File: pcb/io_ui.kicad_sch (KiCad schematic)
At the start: 27 parts, among them J10 UART, J4 Digital IO, J5 ADC Inputs, J8 I2C Bus, Q4 2N7002, Q5 2N7002, U6 128x32 OLED, U8 24AA64T

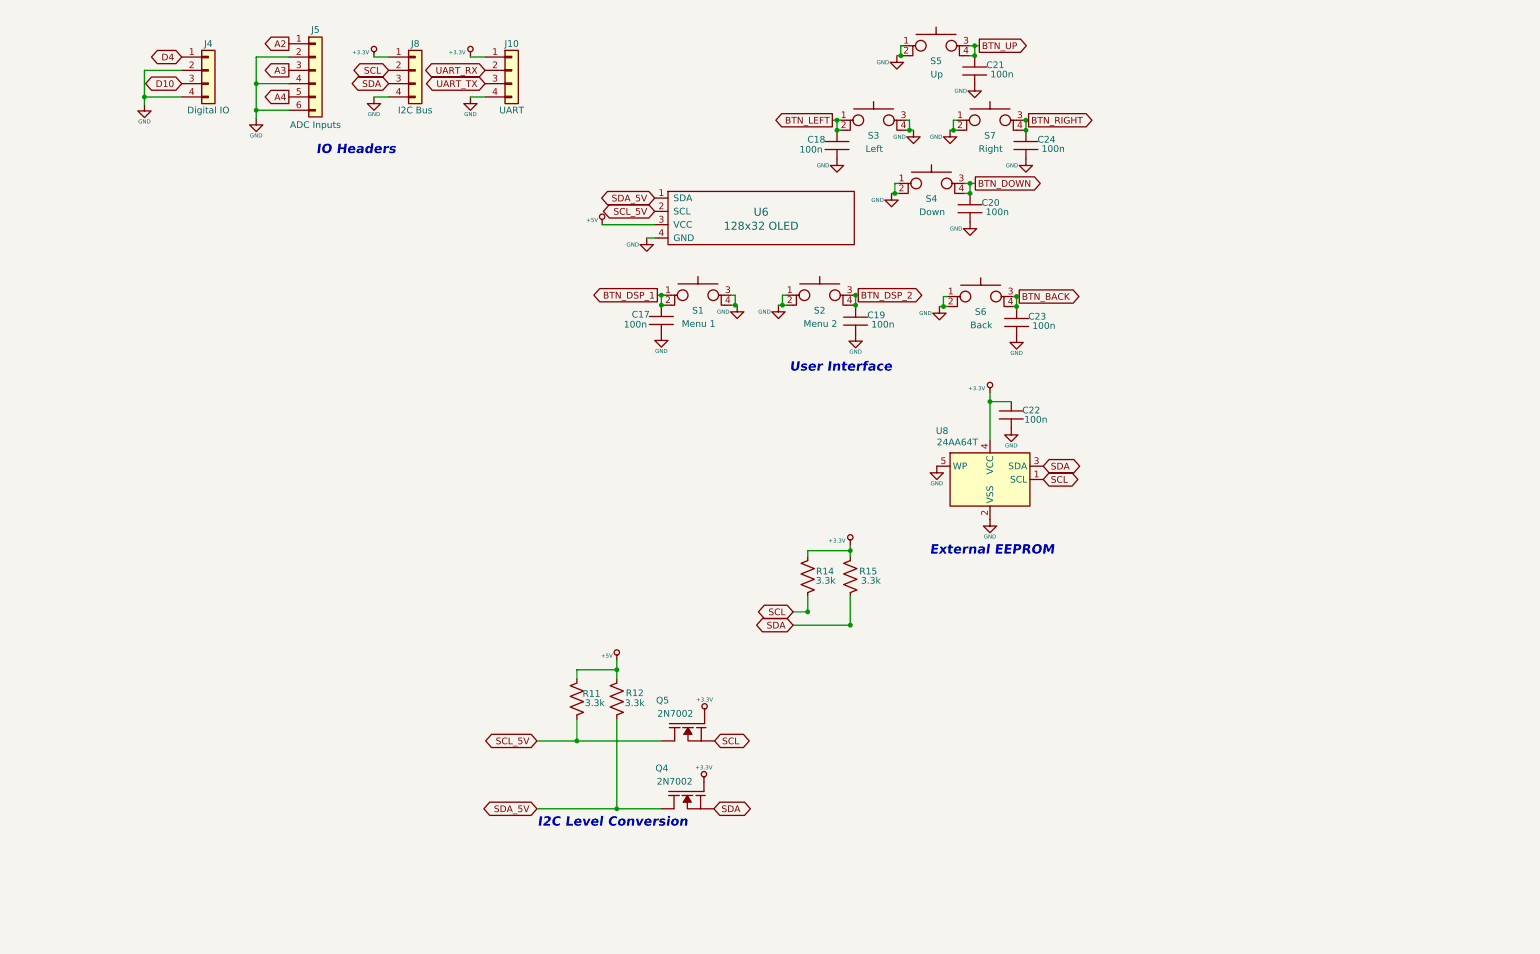
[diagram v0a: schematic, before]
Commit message: UI: 128x32 I2C OLED -> 1.3in SH1106 SPI 7-pin DS1 (as Si5351AVFO, DNP) on SPI1 ALT1 PC4/PC6 + CS PC7, DC PB4, RES PB5; FB1+C25-C27 rail filter; VFO 10k/10k/100n RC on all 7 buttons (R50-R63); D-pad stays PD3-PD6; layout note; regen PDF
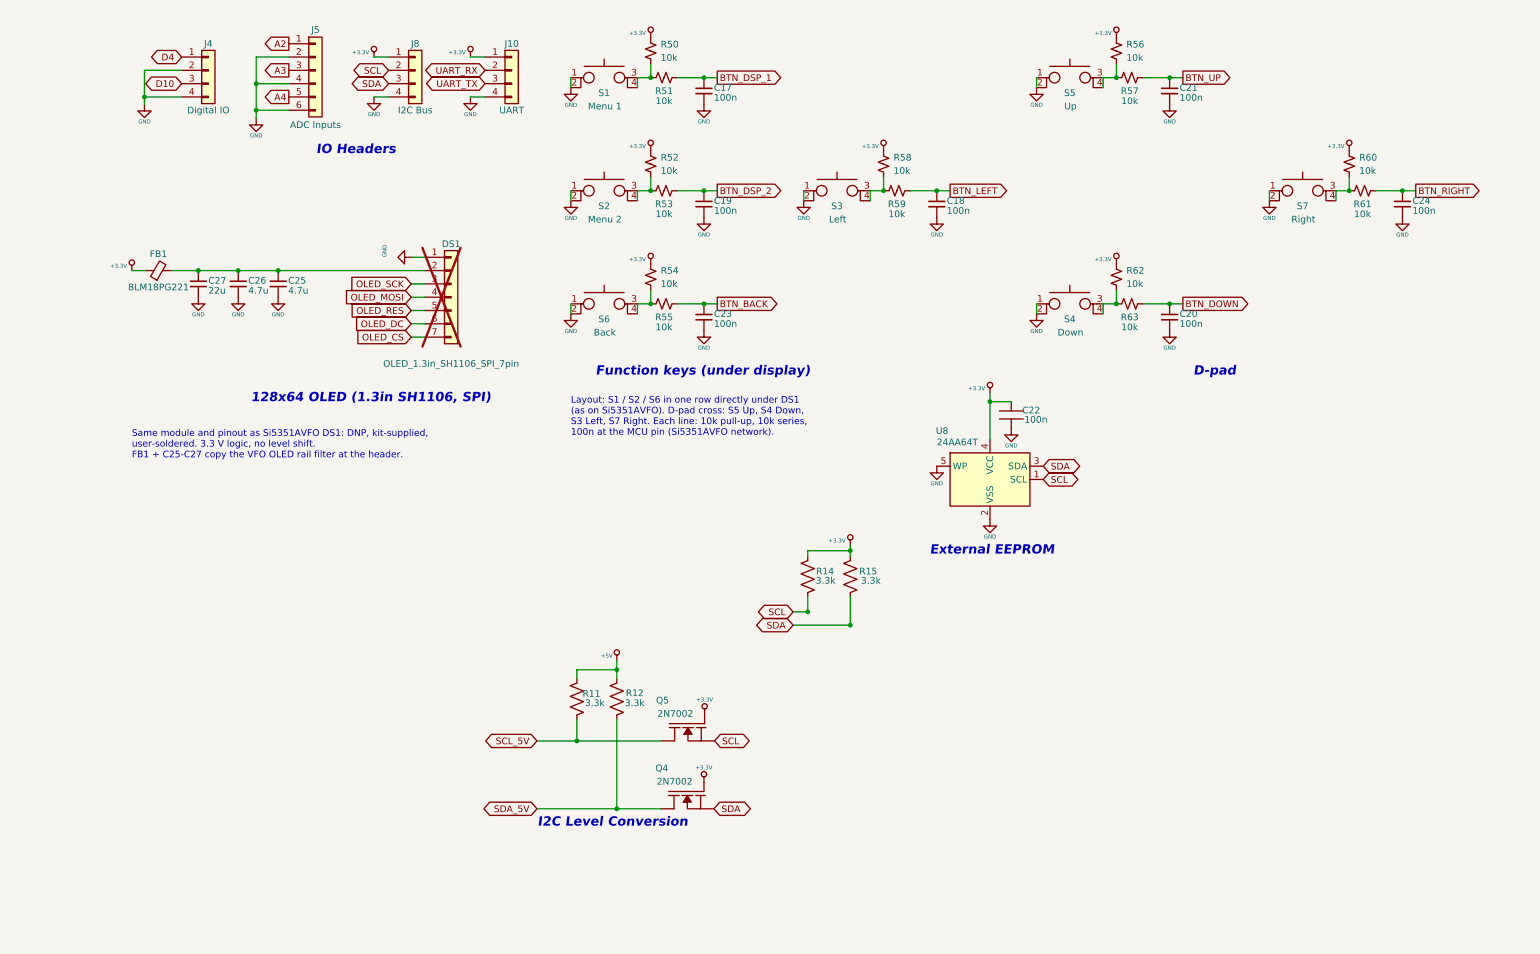
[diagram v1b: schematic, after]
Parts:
- removed C17, C18, C19, C20, C21, C23, C24: 100n, Capacitor_SMD:C_0805_2012Metric, symbol EtherkitKicadLibrary:C
- removed U6: 128x32 OLED, EtherkitKicadLibrary:128x32OLED, symbol EtherkitKicadLibrary:128x32OLED
- added C17, C18, C19, C20, C21, C23, C24: 100n, Capacitor_SMD:C_0805_2012Metric, symbol Device:C_Small
- added C25, C26: 4.7u, Capacitor_SMD:C_0805_2012Metric, symbol Device:C_Small
- added C27: 22u, Capacitor_SMD:C_1206_3216Metric, symbol Device:C_Small
- added DS1: OLED_1.3in_SH1106_SPI_7pin, Connector_PinHeader_2.54mm:PinHeader_1x07_P2.54mm_Vertical, symbol Connector_Generic:Conn_01x07
- added FB1: BLM18PG221, Inductor_SMD:L_0603_1608Metric, symbol Device:FerriteBead_Small
- added R50, R51, R52, R53, R54, R55, R56, R57, R58, R59, R60, R61, R62, R63: 10k, Resistor_SMD:R_0805_2012Metric, symbol Device:R_Small_US
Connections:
- net +3.3V: now also FB1.1, R50.1, R52.1, R54.1, R56.1, R58.1, R60.1, R62.1
- net BTN_BACK: now also C23.1, R55.2; no longer S6.3, S6.4
- net BTN_DOWN: now also C20.1, R63.2; no longer S4.3, S4.4
- net BTN_DSP_1: now also C17.1, R51.2; no longer S1.1, S1.2
- net BTN_DSP_2: now also C19.1, R53.2; no longer S2.3, S2.4
- net BTN_LEFT: now also C18.1, R59.2; no longer S3.1, S3.2
- net BTN_RIGHT: now also C24.1, R61.2; no longer S7.3, S7.4
- net BTN_UP: now also C21.1, R57.2; no longer S5.3, S5.4
- net GND: now also S1.1, S1.2, S3.1, S3.2, C17.2, C18.2, C19.2, C20.2, C21.2, C23.2, C24.2, C25.2, C26.2, C27.2, DS1.1 (Pin_1); no longer S1.3, S1.4, S3.3, S3.4
- new net: R56.2, R57.1, S5.3, S5.4
- new net: R58.2, R59.1, S3.3, S3.4
- new net: R60.2, R61.1, S7.3, S7.4
- new net: R62.2, R63.1, S4.3, S4.4
- new net: R50.2, R51.1, S1.3, S1.4
- new net: R52.2, R53.1, S2.3, S2.4
- new net: R54.2, R55.1, S6.3, S6.4
- new net: C25.1, C26.1, C27.1, DS1.2 (Pin_2), FB1.2
- new net OLED_CS: DS1.7 (Pin_7)
- new net OLED_DC: DS1.6 (Pin_6)
- new net OLED_MOSI: DS1.4 (Pin_4)
- new net OLED_RES: DS1.5 (Pin_5)
- new net OLED_SCK: DS1.3 (Pin_3)
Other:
- note added: "128x64 OLED (1.3in SH1106, SPI)"
- note added: "D-pad"
- note added: "Function keys (under display)"
- note added: "Layout: S1 / S2 / S6 in one row directly under DS1 (as on Si5351AVFO). D-pad cross: S5 Up, S4 Down, S3 Left, S7 Right. Each line: 10k pull-up, 10k series, 100n at the MCU pin (Si5351AVFO network)."
- note added: "Same module and pinout as Si5351AVFO DS1: DNP, kit-supplied, user-soldered. 3.3 V logic, no level shift. FB1 + C25-C27 copy the VFO OLED rail filter at the header."
- note removed: "User Interface"
- moved on the sheet: S1, S2, S3, S4, S5, S6, S7

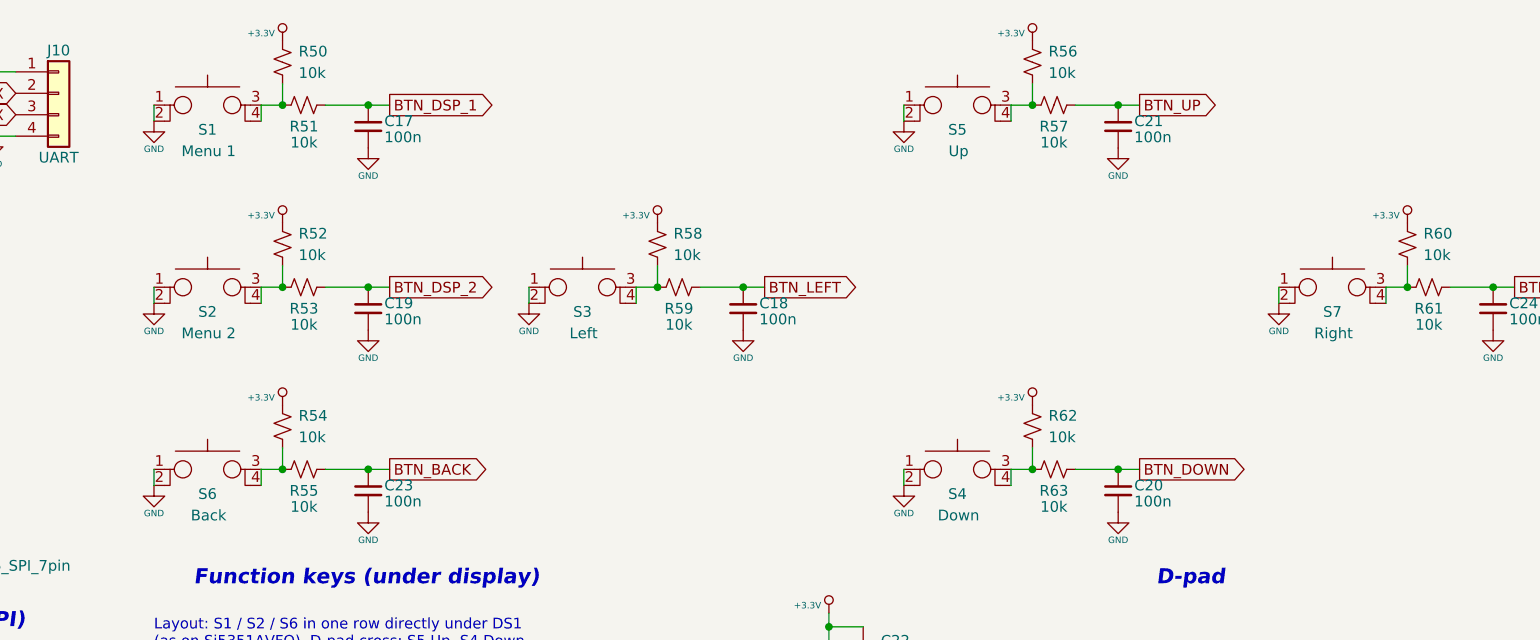
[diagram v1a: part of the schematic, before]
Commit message: UI: S1-S7 Omron B3F (4-pin) -> Kinghelm KH-6X6X11H-STM C2837537 as on Si5351AVFO (Switch:SW_Push 2-pin, OB2:SW_Push_6x6mm_SMD_KH-6X6X11H-STM footprint copied from VFO lib); pin1=GND, pin2=RC net; nets unchanged; regen PDF
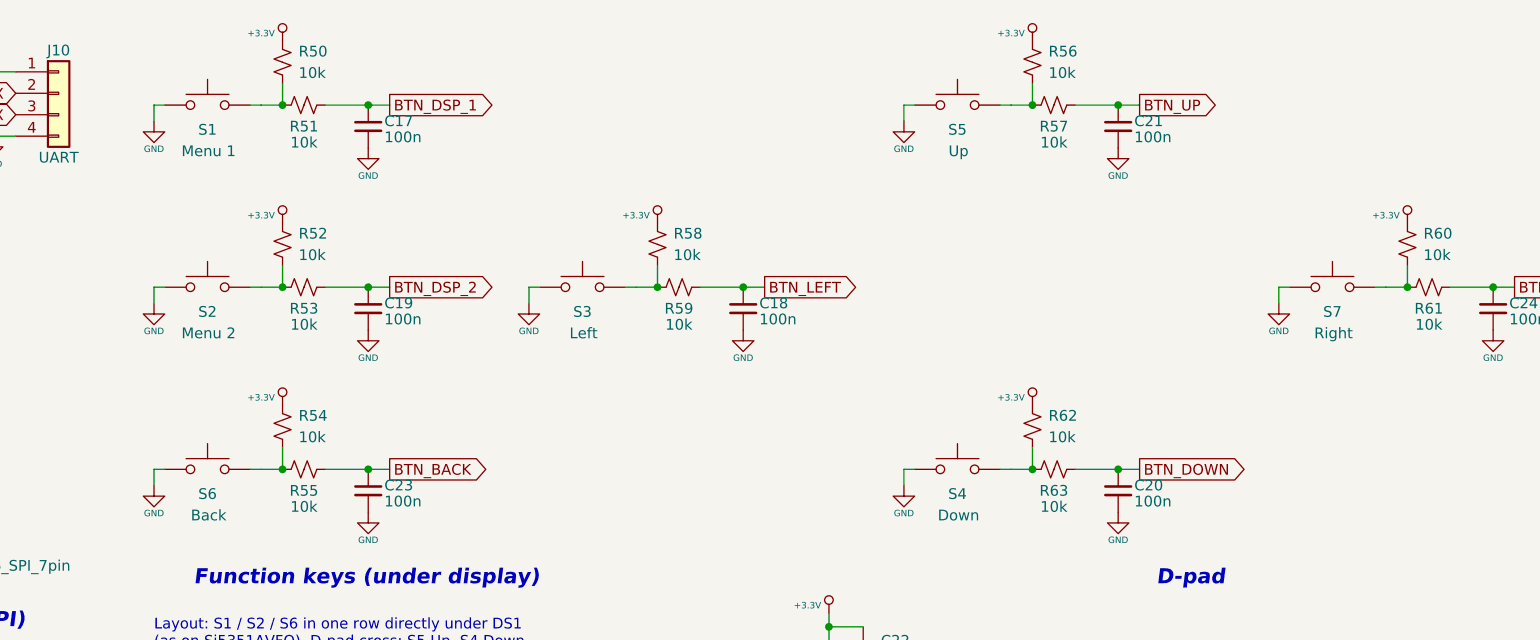
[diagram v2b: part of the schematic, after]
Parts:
- S1, S2, S3, S4, S5, S6, S7: footprint EtherkitKicadLibrary:Omron_B3F-1052 -> OB2:SW_Push_6x6mm_SMD_KH-6X6X11H-STM; symbol EtherkitKicadLibrary:PUSHBUTTON_TACTILE -> Switch:SW_Push; LCSC (none) -> C2837537; MPN (none) -> KH-6X6X11H-STM; Manufacturer (none) -> Kinghelm
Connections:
- net GND: no longer S1.2, S2.2, S3.2, S4.2, S5.2, S6.2, S7.2
- net at R56.2, R57.1: now also S5.2; no longer S5.3, S5.4
- net at R58.2, R59.1: now also S3.2; no longer S3.3, S3.4
- net at R60.2, R61.1: now also S7.2; no longer S7.3, S7.4
- net at R62.2, R63.1: now also S4.2; no longer S4.3, S4.4
- net at R50.2, R51.1: now also S1.2; no longer S1.3, S1.4
- net at R52.2, R53.1: now also S2.2; no longer S2.3, S2.4
- net at R54.2, R55.1: now also S6.2; no longer S6.3, S6.4

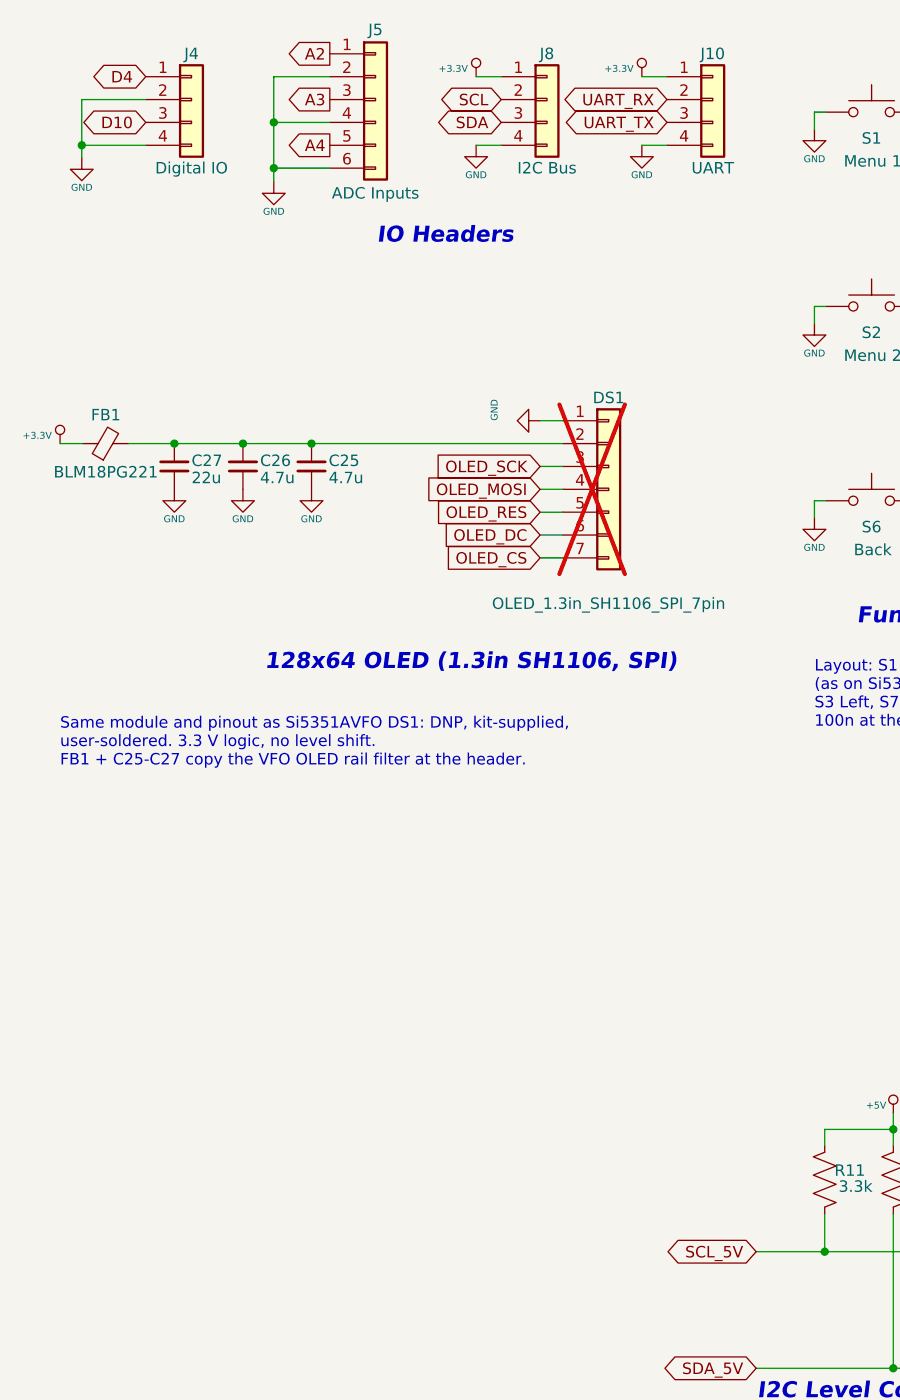
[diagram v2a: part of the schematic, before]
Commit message: IO: Option B spare GPIO - J4 1x10 (D7/PA7, D17/PC3, D19/PC5, D38/A20/PF4, D39/A21/PF5, GND between), J5 1x12 (D22-D24/A0-A2/PD0-PD2, D31-D33/A9-A11/PE1-PE3, GND between); DxCore 48pin-standard net names; NC flags removed from PC5/PE1-3/PF4/PF5; J8/J10 shifted left; regen PDF
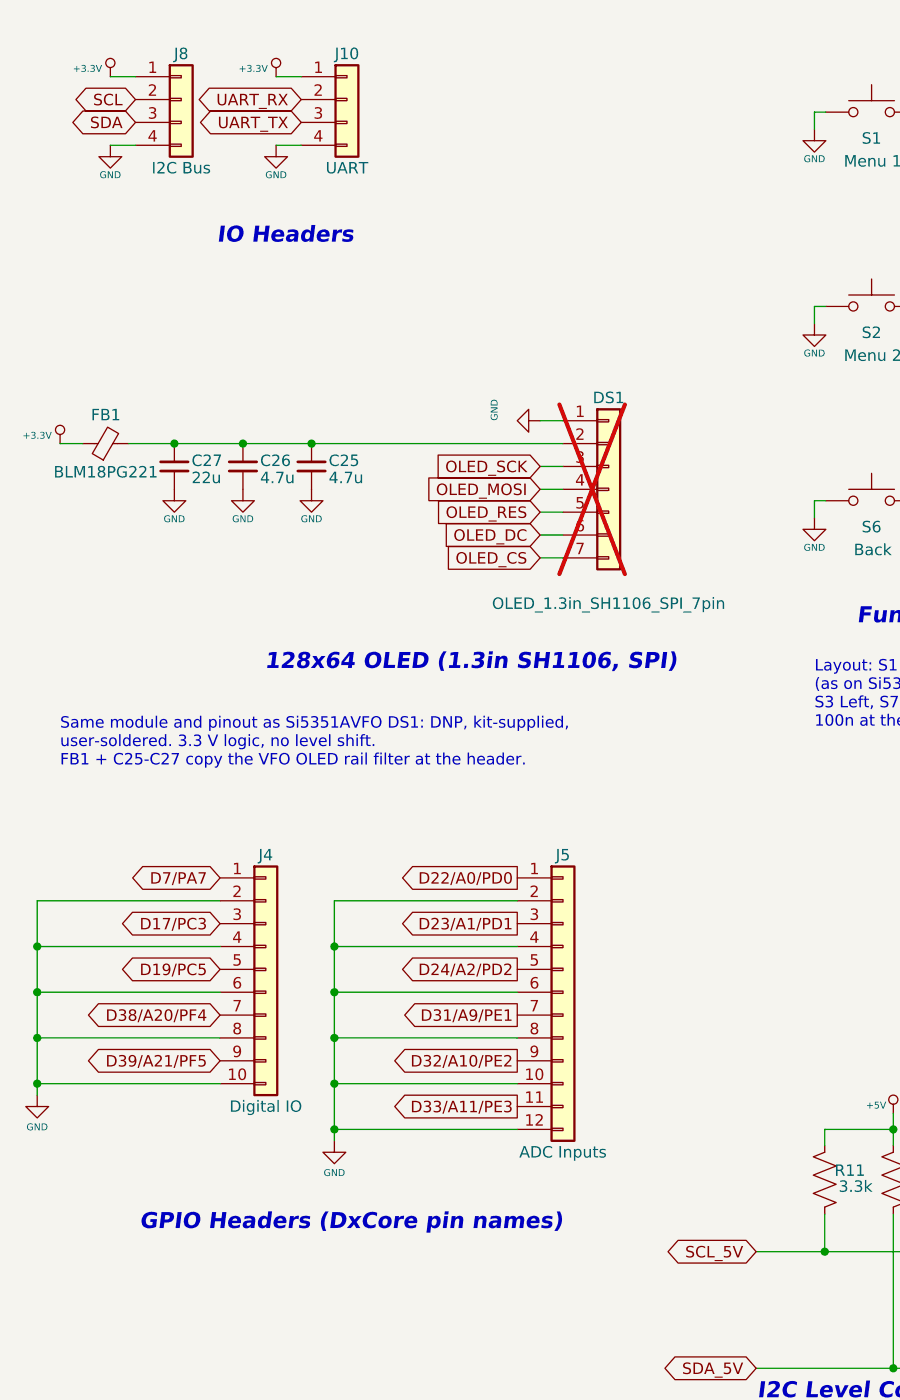
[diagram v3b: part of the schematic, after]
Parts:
- J4: footprint Connector_PinHeader_2.54mm:PinHeader_1x04_P2.54mm_Vertical -> Connector_PinHeader_2.54mm:PinHeader_1x10_P2.54mm_Vertical; symbol Connector_Generic:Conn_01x04 -> Connector_Generic:Conn_01x10
- J5: footprint Connector_PinHeader_2.54mm:PinHeader_1x06_P2.54mm_Vertical -> Connector_PinHeader_2.54mm:PinHeader_1x12_P2.54mm_Vertical; symbol Connector_Generic:Conn_01x06 -> Connector_Generic:Conn_01x12
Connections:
- net GND: now also J4.10 (Pin_10), J4.6 (Pin_6), J4.8 (Pin_8), J5.10 (Pin_10), J5.12 (Pin_12), J5.8 (Pin_8)
- net A2 renamed D22/A0/PD0
- net A3 renamed D23/A1/PD1
- net A4 renamed D24/A2/PD2
- net D10 renamed D17/PC3
- net D4 renamed D7/PA7
- new net D19/PC5: J4.5 (Pin_5)
- new net D31/A9/PE1: J5.7 (Pin_7)
- new net D32/A10/PE2: J5.9 (Pin_9)
- new net D33/A11/PE3: J5.11 (Pin_11)
- new net D38/A20/PF4: J4.7 (Pin_7)
- new net D39/A21/PF5: J4.9 (Pin_9)
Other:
- note added: "GPIO Headers (DxCore pin names)"
- moved on the sheet: J10, J8

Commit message: IO: header GPIO net labels slash -> underscore (D7_PA7, D22_A0_PD0, ...); renames only; regen PDF
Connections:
- net D17/PC3 renamed D17_PC3
- net D19/PC5 renamed D19_PC5
- net D22/A0/PD0 renamed D22_A0_PD0
- net D23/A1/PD1 renamed D23_A1_PD1
- net D24/A2/PD2 renamed D24_A2_PD2
- net D31/A9/PE1 renamed D31_A9_PE1
- net D32/A10/PE2 renamed D32_A10_PE2
- net D33/A11/PE3 renamed D33_A11_PE3
- net D38/A20/PF4 renamed D38_A20_PF4
- net D39/A21/PF5 renamed D39_A21_PF5
- net D7/PA7 renamed D7_PA7
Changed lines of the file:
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@@
 		)
 	)
-	(global_label "D7/PA7"
+	(global_label "D7_PA7"
 		(shape bidirectional)
 		(at 35.56 111.76 180)
@@
 		)
 	)
-	(global_label "D17/PC3"
+	(global_label "D17_PC3"
 		(shape bidirectional)
 		(at 35.56 116.84 180)
@@
 		)
 	)
-	(global_label "D19/PC5"
+	(global_label "D19_PC5"
 		(shape bidirectional)
 		(at 35.56 121.92 180)
@@
 		)
 	)
-	(global_label "D38/A20/PF4"
+	(global_label "D38_A20_PF4"
 		(shape bidirectional)
 		(at 35.56 127 180)
@@
 		)
 	)
-	(global_label "D39/A21/PF5"
+	(global_label "D39_A21_PF5"
 		(shape bidirectional)
 		(at 35.56 132.08 180)
@@
 		)
 	)
-	(global_label "D22/A0/PD0"
+	(global_label "D22_A0_PD0"
 		(shape output)
 		(at 68.58 111.76 180)
@@
 		)
 	)
-	(global_label "D23/A1/PD1"
+	(global_label "D23_A1_PD1"
 		(shape output)
 		(at 68.58 116.84 180)
@@
 		)
 	)
-	(global_label "D24/A2/PD2"
+	(global_label "D24_A2_PD2"
 		(shape output)
 		(at 68.58 121.92 180)
@@
 		)
 	)
-	(global_label "D31/A9/PE1"
+	(global_label "D31_A9_PE1"
 		(shape output)
 		(at 68.58 127 180)
@@
 		)
 	)
-	(global_label "D32/A10/PE2"
+	(global_label "D32_A10_PE2"
 		(shape output)
 		(at 68.58 132.08 180)
@@
 		)
 	)
-	(global_label "D33/A11/PE3"
+	(global_label "D33_A11_PE3"
 		(shape output)
 		(at 68.58 137.16 180)
